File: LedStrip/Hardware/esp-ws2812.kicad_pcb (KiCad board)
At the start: 2 copper layers, 32 x 12 mm, 14 parts, among them P1 CONN_01X02, P2 CONN_01X04, P3 CONN_01X01, P4 CONN_01X02, Q1 BSS138, U1 MCP1700, U2 ESP-01v090

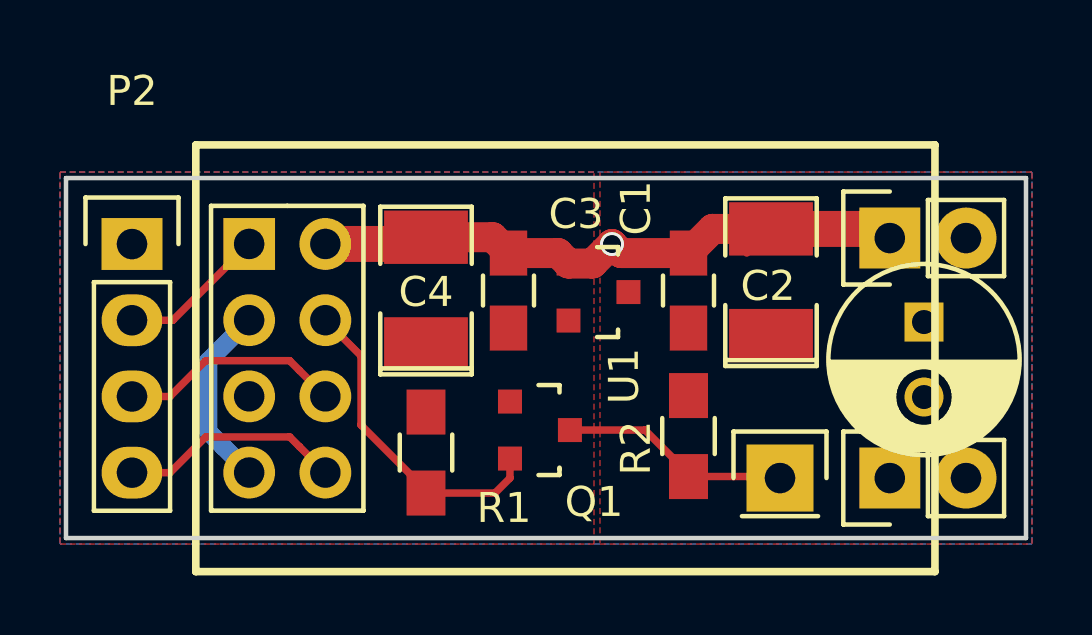
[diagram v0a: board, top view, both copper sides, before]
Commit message: small board update for metric tant layouts
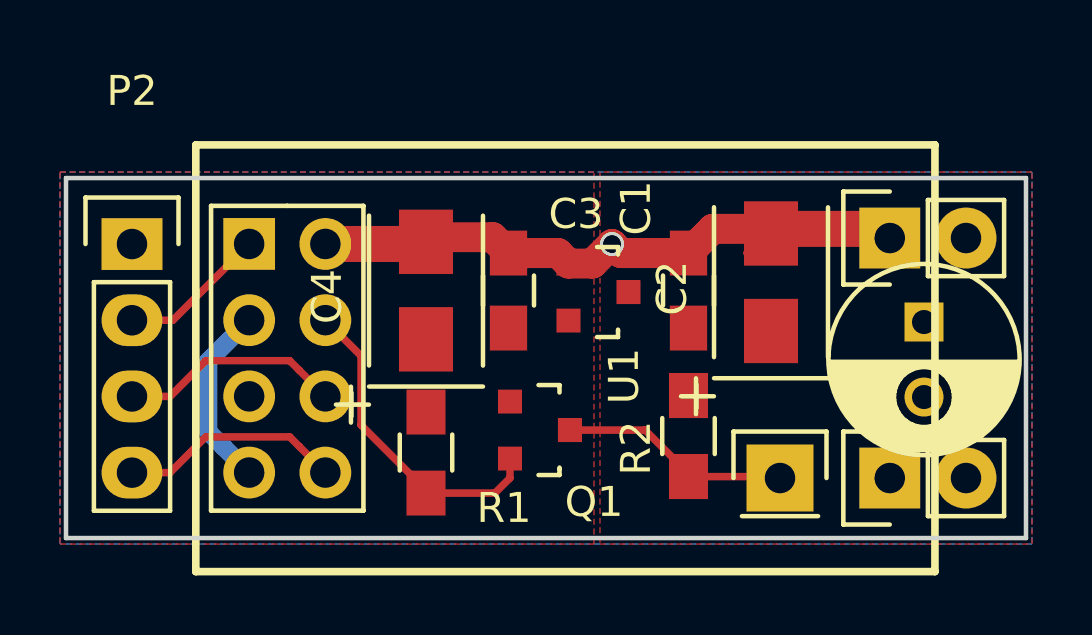
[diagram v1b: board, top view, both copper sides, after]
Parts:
- C2, C4: footprint SMD_Packages:SMD-1210_Pol -> Capacitors_Tantalum_SMD:TantalC_SizeB_EIA-3528_Wave
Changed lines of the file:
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@@
   (layers
     (0 F.Cu signal)
-    (31 B.Cu signal hide)
+    (31 B.Cu signal)
     (32 B.Adhes user)
     (33 F.Adhes user)
@@
     )
   )
-  (module SMD_Packages:SMD-1210_Pol (layer F.Cu)
-    (at 158 93.75 90)
-    (tags "CMS SM")
-    (attr smd)
-    (fp_text reference C4 (at -0.05 0 360) (layer F.SilkS)
-      (effects (font (size 1 1) (thickness 0.15)))
-    )
-    (fp_text value 2.2uf (at 5.75 0 90) (layer F.Fab)
-      (effects (font (size 1 1) (thickness 0.15)))
-    )
-    (fp_line (start -2.794 -1.524) (end -2.794 1.524) (layer F.SilkS) (width 0.15))
-    (fp_line (start 0.889 1.524) (end 2.794 1.524) (layer F.SilkS) (width 0.15))
-    (fp_line (start 2.794 1.524) (end 2.794 -1.524) (layer F.SilkS) (width 0.15))
-    (fp_line (start 2.794 -1.524) (end 0.889 -1.524) (layer F.SilkS) (width 0.15))
-    (fp_line (start -0.762 -1.524) (end -2.794 -1.524) (layer F.SilkS) (width 0.15))
-    (fp_line (start -2.594 -1.524) (end -2.594 1.524) (layer F.SilkS) (width 0.15))
-    (fp_line (start -2.794 1.524) (end -0.762 1.524) (layer F.SilkS) (width 0.15))
-    (pad 1 smd rect (at -1.778 0 90) (size 1.778 2.794) (layers F.Cu F.Paste F.Mask)
-      (net 3 +3V3))
-    (pad 2 smd rect (at 1.778 0 90) (size 1.778 2.794) (layers F.Cu F.Paste F.Mask)
-      (net 2 GND))
-    (model SMD_Packages.3dshapes/SMD-1210_Pol.wrl
-      (at (xyz 0 0 0))
-      (scale (xyz 0.2 0.2 0.2))
-      (rotate (xyz 0 0 0))
-    )
-  )
   (module Pin_Headers:Pin_Header_Straight_1x01 (layer F.Cu)
     (at 169.8 100)
@@
       (scale (xyz 1 1 1))
       (rotate (xyz 0 0 90))
-    )
-  )
-  (module SMD_Packages:SMD-1210_Pol (layer F.Cu)
-    (at 169.5 93.472 90)
-    (tags "CMS SM")
-    (attr smd)
-    (fp_text reference C2 (at -0.128 -0.1 180) (layer F.SilkS)
-      (effects (font (size 1 1) (thickness 0.15)))
-    )
-    (fp_text value 2.2uf (at 0 0.762 90) (layer F.Fab)
-      (effects (font (size 1 1) (thickness 0.15)))
-    )
-    (fp_line (start -2.794 -1.524) (end -2.794 1.524) (layer F.SilkS) (width 0.15))
-    (fp_line (start 0.889 1.524) (end 2.794 1.524) (layer F.SilkS) (width 0.15))
-    (fp_line (start 2.794 1.524) (end 2.794 -1.524) (layer F.SilkS) (width 0.15))
-    (fp_line (start 2.794 -1.524) (end 0.889 -1.524) (layer F.SilkS) (width 0.15))
-    (fp_line (start -0.762 -1.524) (end -2.794 -1.524) (layer F.SilkS) (width 0.15))
-    (fp_line (start -2.594 -1.524) (end -2.594 1.524) (layer F.SilkS) (width 0.15))
-    (fp_line (start -2.794 1.524) (end -0.762 1.524) (layer F.SilkS) (width 0.15))
-    (pad 1 smd rect (at -1.778 0 90) (size 1.778 2.794) (layers F.Cu F.Paste F.Mask)
-      (net 1 +5V))
-    (pad 2 smd rect (at 1.778 0 90) (size 1.778 2.794) (layers F.Cu F.Paste F.Mask)
-      (net 2 GND))
-    (model SMD_Packages.3dshapes/SMD-1210_Pol.wrl
-      (at (xyz 0 0 0))
-      (scale (xyz 0.2 0.2 0.2))
-      (rotate (xyz 0 0 0))
     )
   )
@@
     )
   )
+  (module Capacitors_Tantalum_SMD:TantalC_SizeB_EIA-3528_Wave (layer F.Cu)
+    (at 158 93.75 90)
+    (descr "Tantal Cap. , Size B, EIA-3528, Wave,")
+    (tags "Tantal Cap. , Size B, EIA-3528, Wave,")
+    (attr smd)
+    (fp_text reference C4 (at -0.20066 -3.29946 90) (layer F.SilkS)
+      (effects (font (size 1 1) (thickness 0.15)))
+    )
+    (fp_text value 2.2uf (at -0.09906 3.59918 90) (layer F.Fab)
+      (effects (font (size 1 1) (thickness 0.15)))
+    )
+    (fp_text user + (at -3.79984 -2.49936 90) (layer F.SilkS)
+      (effects (font (size 1 1) (thickness 0.15)))
+    )
+    (fp_line (start -3.2004 -1.89992) (end -3.2004 1.89992) (layer F.SilkS) (width 0.15))
+    (fp_line (start 2.49936 -1.89992) (end -2.49936 -1.89992) (layer F.SilkS) (width 0.15))
+    (fp_line (start 2.49682 1.89992) (end -2.5019 1.89992) (layer F.SilkS) (width 0.15))
+    (fp_line (start -3.80238 -3.00228) (end -3.80238 -1.90246) (layer F.SilkS) (width 0.15))
+    (fp_line (start -4.40182 -2.5019) (end -3.20294 -2.5019) (layer F.SilkS) (width 0.15))
+    (pad 2 smd rect (at 1.6256 0 90) (size 2.14884 1.80086) (layers F.Cu F.Paste F.Mask)
+      (net 2 GND))
+    (pad 1 smd rect (at -1.6256 0 90) (size 2.14884 1.80086) (layers F.Cu F.Paste F.Mask)
+      (net 3 +3V3))
+    (model Capacitors_Tantalum_SMD.3dshapes/TantalC_SizeB_EIA-3528_Wave.wrl
+      (at (xyz 0 0 0))
+      (scale (xyz 1 1 1))
+      (rotate (xyz 0 0 180))
+    )
+  )
+  (module Capacitors_Tantalum_SMD:TantalC_SizeB_EIA-3528_Wave (layer F.Cu)
+    (at 169.5 93.472 90)
+    (descr "Tantal Cap. , Size B, EIA-3528, Wave,")
+    (tags "Tantal Cap. , Size B, EIA-3528, Wave,")
+    (attr smd)
+    (fp_text reference C2 (at -0.20066 -3.29946 90) (layer F.SilkS)
+      (effects (font (size 1 1) (thickness 0.15)))
+    )
+    (fp_text value 2.2uf (at -0.09906 3.59918 90) (layer F.Fab)
+      (effects (font (size 1 1) (thickness 0.15)))
+    )
+    (fp_text user + (at -3.79984 -2.49936 90) (layer F.SilkS)
+      (effects (font (size 1 1) (thickness 0.15)))
+    )
+    (fp_line (start -3.2004 -1.89992) (end -3.2004 1.89992) (layer F.SilkS) (width 0.15))
+    (fp_line (start 2.49936 -1.89992) (end -2.49936 -1.89992) (layer F.SilkS) (width 0.15))
+    (fp_line (start 2.49682 1.89992) (end -2.5019 1.89992) (layer F.SilkS) (width 0.15))
+    (fp_line (start -3.80238 -3.00228) (end -3.80238 -1.90246) (layer F.SilkS) (width 0.15))
+    (fp_line (start -4.40182 -2.5019) (end -3.20294 -2.5019) (layer F.SilkS) (width 0.15))
+    (pad 2 smd rect (at 1.6256 0 90) (size 2.14884 1.80086) (layers F.Cu F.Paste F.Mask)
+      (net 2 GND))
+    (pad 1 smd rect (at -1.6256 0 90) (size 2.14884 1.80086) (layers F.Cu F.Paste F.Mask)
+      (net 1 +5V))
+    (model Capacitors_Tantalum_SMD.3dshapes/TantalC_SizeB_EIA-3528_Wave.wrl
+      (at (xyz 0 0 0))
+      (scale (xyz 1 1 1))
+      (rotate (xyz 0 0 180))
+    )
+  )
